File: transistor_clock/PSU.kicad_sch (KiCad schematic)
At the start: 15 parts, among them Q125 TIP41, Q27 MMBT3904

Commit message: seconds_minor_wrapup
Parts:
- C74, C76, D255, RV1: Assembly (none) -> False
- D296: footprint (none) -> Package_SO:SO-4_4.4x4.3mm_P2.54mm; Assembly (none) -> False
- D297: footprint (none) -> Diode_SMD:D_MiniMELF; Assembly (none) -> False
- Q123, Q124: renamed from Q27; Assembly (none) -> True; LCSC_PN (none) -> C20526; Price (none) -> 0.0094
- R20: renamed from R45; LCSC_PN (none) -> C21190; Price (none) -> 0.0005
- renumbered R45 to R20, R20 to R243, R41 to R253

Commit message: seconds_major_wrapup
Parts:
- R20: Assembly (none) -> True
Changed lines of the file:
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@@
       (effects (font (size 1.27 1.27)) hide)
     )
-    (property "Assembly" "" (at 157.48 76.2 0)
+    (property "Assembly" "True" (at 157.48 76.2 0)
       (effects (font (size 1.27 1.27)) hide)
     )
@@
       (effects (font (size 1.27 1.27)) hide)
     )
-    (property "Assembly" "" (at 132.08 77.47 0)
-      (effects (font (size 1.27 1.27)) hide)
-    )
+    (property "Assembly" "True" (at 132.08 77.47 0)
+      (effects (font (size 1.27 1.27)) hide)
+    )

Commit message: added content
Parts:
- C76: value 100u -> 10u; footprint (none) -> Capacitor_SMD:C_0805_2012Metric; Assembly False -> True; LCSC_PN (none) -> C15850; Price (none) -> 0.0105

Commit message: added content
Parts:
- removed D255: LED, LED_SMD:LED_0603_1608Metric, symbol Device:LED
- removed Q124: MMBT3904, Package_TO_SOT_SMD:SOT-23, symbol Transistor_BJT:MMBT3904
- removed R20 (x2): 1k, Resistor_SMD:R_0603_1608Metric, symbol Device:R
- removed R243, R253: 500, Resistor_SMD:R_0603_1608Metric, symbol Device:R
- removed RV1: 500, symbol Device:R_Potentiometer
- added C60, C65, C66, C81, C82: 10u, Capacitor_SMD:C_1206_3216Metric, symbol Device:C_Polarized
- added C61: 10u, Capacitor_SMD:C_0805_2012Metric, symbol Device:C_Polarized
- added D144: 1N4148W, Diode_SMD:D_SOD-123, symbol Device:D
- C74: footprint (none) -> Capacitor_THT:CP_Radial_D10.0mm_P3.50mm
- C75: value 220u -> 10u; footprint (none) -> Capacitor_SMD:C_1206_3216Metric; Assembly (none) -> True; LCSC_PN (none) -> C13585; Price (none) -> 0.029
- D297: value D_Zener -> 11V
- Q125: footprint Package_TO_SOT_THT:TO-220-3_Vertical -> Package_TO_SOT_THT:TO-220-3_Horizontal_TabDown
- R20: value 500 -> 1k; Assembly (none) -> True; LCSC_PN (none) -> C21190; Price (none) -> 0.0005
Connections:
- net 12V_out: now also C61.1
- net GND: now also C60.2, C61.2, C65.2, C66.2, C81.2, C82.2
- net at Q123.1 (B): now also R20.2, C82.1, D144.2 (A)
- net at C75.1: now also C74.1, D296.1 (+), Q123.3 (C), Q125.2 (C), R20.1, C60.1, C65.1, C66.1, C81.1; no longer R20.2
- net at D297.1 (K): now also D144.1 (K)
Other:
- moved on the sheet: C76, D297, Q123, Q125, R20

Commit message: added content
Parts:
- added C83, C84, C97: 10u, Capacitor_SMD:C_1206_3216Metric, symbol Device:C_Polarized
- C74: value 10mF -> 220u
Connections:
- net GND: now also C83.2, C84.2, C97.2
- net at C60.1, C65.1, C66.1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: now also C83.1, C84.1, C97.1
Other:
- note added: "TODO check tran"
- note removed: "Check tran/replace with darlington?"
- moved on the sheet: C61, C75, C76, C82, D144, D297, Q123, Q125, R20

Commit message: added content
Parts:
- renumbered D144 to D139
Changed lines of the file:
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@@
   (symbol (lib_id "Device:D") (at 185.42 73.66 90) (unit 1)
     (in_bom yes) (on_board yes) (dnp no) (fields_autoplaced)
-    (property "Reference" "D144" (at 187.452 73.0163 90)
+    (property "Reference" "D139" (at 187.452 73.0163 90)
       (effects (font (size 1.27 1.27)) (justify right))
     )
@@
     (instances
       (project "transistor_clock"
-        (path "/b32464e6-c3c7-41da-ac79-643e545075e2/7ea6f02c-98d6-4cc3-9d12-1d5708d2f4a9/cadfc701-a229-43d0-bd3d-a4fb656a51ec/cdd346a2-af99-4cba-a870-25a15852fcab"
-          (reference "D144") (unit 1)
+        (path "/b32464e6-c3c7-41da-ac79-643e545075e2/fc84256b-6a0b-4a66-8a9d-3464331d8c4b/cadfc701-a229-43d0-bd3d-a4fb656a51ec/cdd346a2-af99-4cba-a870-25a15852fcab"
+          (reference "D139") (unit 1)
+        )
+        (path "/b32464e6-c3c7-41da-ac79-643e545075e2/fc837116-7951-4754-b134-6b29a9ce0d20/f7326efb-cfc5-42e3-bc99-3d82c7965823/09ad6700-0804-43e5-8393-34ed739096ca"
+          (reference "D302") (unit 1)
+        )
+        (path "/b32464e6-c3c7-41da-ac79-643e545075e2/fc84256b-6a0b-4a66-8a9d-3464331d8c4b/cadfc701-a229-43d0-bd3d-a4fb656a51ec/7f89f7e8-4eb0-459f-8749-acca2517c0c8"
+          (reference "D256") (unit 1)
+        )
+        (path "/b32464e6-c3c7-41da-ac79-643e545075e2/369b0561-6154-45b1-b267-ff673911a7b5/f7326efb-cfc5-42e3-bc99-3d82c7965823/96f657b6-18d3-41c6-a281-d64d12e655e8"
+          (reference "D298") (unit 1)
+        )
+        (path "/b32464e6-c3c7-41da-ac79-643e545075e2/369b0561-6154-45b1-b267-ff673911a7b5/f7326efb-cfc5-42e3-bc99-3d82c7965823/4e2cbe41-dc2d-4674-8cd4-acbdb09cdaf2"
+          (reference "D299") (unit 1)
+        )
+        (path "/b32464e6-c3c7-41da-ac79-643e545075e2/fc84256b-6a0b-4a66-8a9d-3464331d8c4b/cadfc701-a229-43d0-bd3d-a4fb656a51ec/0211eb0b-97a3-455a-a4b9-49336bda2571"
+          (reference "D141") (unit 1)
+        )
+        (path "/b32464e6-c3c7-41da-ac79-643e545075e2/7ea6f02c-98d6-4cc3-9d12-1d5708d2f4a9/cadfc701-a229-43d0-bd3d-a4fb656a51ec/0211eb0b-97a3-455a-a4b9-49336bda2571"
+          (reference "D142") (unit 1)
+        )
+        (path "/b32464e6-c3c7-41da-ac79-643e545075e2/fc837116-7951-4754-b134-6b29a9ce0d20/f7326efb-cfc5-42e3-bc99-3d82c7965823/df4d8492-d3b8-496d-b6ec-19710c264b23"
+          (reference "D303") (unit 1)
+        )
+        (path "/b32464e6-c3c7-41da-ac79-643e545075e2/fc84256b-6a0b-4a66-8a9d-3464331d8c4b/cadfc701-a229-43d0-bd3d-a4fb656a51ec/28fcebf3-a860-4674-8b07-a85c9eaa7b85"
+          (reference "D58") (unit 1)
+        )
+        (path "/b32464e6-c3c7-41da-ac79-643e545075e2/369b0561-6154-45b1-b267-ff673911a7b5/f7326efb-cfc5-42e3-bc99-3d82c7965823/ef0016b9-6554-41fb-9e38-165a2c96731c"
+          (reference "D301") (unit 1)
+        )
+        (path "/b32464e6-c3c7-41da-ac79-643e545075e2/fc84256b-6a0b-4a66-8a9d-3464331d8c4b/cadfc701-a229-43d0-bd3d-a4fb656a51ec/97296d8c-1e14-436e-9883-ea2ff2d821d3"
+          (reference "D281") (unit 1)
+        )
+        (path "/b32464e6-c3c7-41da-ac79-643e545075e2/fc84256b-6a0b-4a66-8a9d-3464331d8c4b/cadfc701-a229-43d0-bd3d-a4fb656a51ec"
+          (reference "D22") (unit 1)
+        )
+        (path "/b32464e6-c3c7-41da-ac79-643e545075e2/fc837116-7951-4754-b134-6b29a9ce0d20/f7326efb-cfc5-42e3-bc99-3d82c7965823/96f657b6-18d3-41c6-a281-d64d12e655e8"
+          (reference "D304") (unit 1)
+        )
+        (path "/b32464e6-c3c7-41da-ac79-643e545075e2/fc837116-7951-4754-b134-6b29a9ce0d20/f7326efb-cfc5-42e3-bc99-3d82c7965823/4e2cbe41-dc2d-4674-8cd4-acbdb09cdaf2"
+          (reference "D305") (unit 1)
+        )
+        (path "/b32464e6-c3c7-41da-ac79-643e545075e2/fc837116-7951-4754-b134-6b29a9ce0d20/f7326efb-cfc5-42e3-bc99-3d82c7965823/b586ad64-4356-4c54-8b14-a38f5ba9b5b3"
+          (reference "D306") (unit 1)
+        )
+        (path "/b32464e6-c3c7-41da-ac79-643e545075e2/fc837116-7951-4754-b134-6b29a9ce0d20/f7326efb-cfc5-42e3-bc99-3d82c7965823/ef0016b9-6554-41fb-9e38-165a2c96731c"
+          (reference "D307") (unit 1)
+        )
+        (path "/b32464e6-c3c7-41da-ac79-643e545075e2/369b0561-6154-45b1-b267-ff673911a7b5/f7326efb-cfc5-42e3-bc99-3d82c7965823/09ad6700-0804-43e5-8393-34ed739096ca"
+          (reference "D296") (unit 1)
+        )
+        (path "/b32464e6-c3c7-41da-ac79-643e545075e2/369b0561-6154-45b1-b267-ff673911a7b5/f7326efb-cfc5-42e3-bc99-3d82c7965823/df4d8492-d3b8-496d-b6ec-19710c264b23"
+          (reference "D297") (unit 1)
+        )
+        (path "/b32464e6-c3c7-41da-ac79-643e545075e2/fc84256b-6a0b-4a66-8a9d-3464331d8c4b/cadfc701-a229-43d0-bd3d-a4fb656a51ec/96e64c28-7545-40f7-aaf3-a4fd012e71a7"
+          (reference "D127") (unit 1)
         )
         (path "/b32464e6-c3c7-41da-ac79-643e545075e2/fc84256b-6a0b-4a66-8a9d-3464331d8c4b/cadfc701-a229-43d0-bd3d-a4fb656a51ec/eec5b1ac-93db-432a-87e8-e2b0529019a6"
@@
           (reference "D285") (unit 1)
         )
-        (path "/b32464e6-c3c7-41da-ac79-643e545075e2/fc84256b-6a0b-4a66-8a9d-3464331d8c4b/cadfc701-a229-43d0-bd3d-a4fb656a51ec/96e64c28-7545-40f7-aaf3-a4fd012e71a7"
-          (reference "D127") (unit 1)
+        (path "/b32464e6-c3c7-41da-ac79-643e545075e2/7ea6f02c-98d6-4cc3-9d12-1d5708d2f4a9/cadfc701-a229-43d0-bd3d-a4fb656a51ec/cdd346a2-af99-4cba-a870-25a15852fcab"
+          (reference "D144") (unit 1)
         )
         (path "/b32464e6-c3c7-41da-ac79-643e545075e2"
@@
           (reference "D300") (unit 1)
         )
-        (path "/b32464e6-c3c7-41da-ac79-643e545075e2/369b0561-6154-45b1-b267-ff673911a7b5/f7326efb-cfc5-42e3-bc99-3d82c7965823/ef0016b9-6554-41fb-9e38-165a2c96731c"
-          (reference "D301") (unit 1)
-        )
-        (path "/b32464e6-c3c7-41da-ac79-643e545075e2/fc837116-7951-4754-b134-6b29a9ce0d20/f7326efb-cfc5-42e3-bc99-3d82c7965823/09ad6700-0804-43e5-8393-34ed739096ca"
-          (reference "D302") (unit 1)
-        )
-        (path "/b32464e6-c3c7-41da-ac79-643e545075e2/fc84256b-6a0b-4a66-8a9d-3464331d8c4b/cadfc701-a229-43d0-bd3d-a4fb656a51ec/7f89f7e8-4eb0-459f-8749-acca2517c0c8"
-          (reference "D256") (unit 1)
-        )
-        (path "/b32464e6-c3c7-41da-ac79-643e545075e2/369b0561-6154-45b1-b267-ff673911a7b5/f7326efb-cfc5-42e3-bc99-3d82c7965823/96f657b6-18d3-41c6-a281-d64d12e655e8"
-          (reference "D298") (unit 1)
-        )
-        (path "/b32464e6-c3c7-41da-ac79-643e545075e2/369b0561-6154-45b1-b267-ff673911a7b5/f7326efb-cfc5-42e3-bc99-3d82c7965823/4e2cbe41-dc2d-4674-8cd4-acbdb09cdaf2"
-          (reference "D299") (unit 1)
-        )
-        (path "/b32464e6-c3c7-41da-ac79-643e545075e2/fc84256b-6a0b-4a66-8a9d-3464331d8c4b/cadfc701-a229-43d0-bd3d-a4fb656a51ec/0211eb0b-97a3-455a-a4b9-49336bda2571"
-          (reference "D141") (unit 1)
-        )
-        (path "/b32464e6-c3c7-41da-ac79-643e545075e2/7ea6f02c-98d6-4cc3-9d12-1d5708d2f4a9/cadfc701-a229-43d0-bd3d-a4fb656a51ec/0211eb0b-97a3-455a-a4b9-49336bda2571"
-          (reference "D142") (unit 1)
-        )
-        (path "/b32464e6-c3c7-41da-ac79-643e545075e2/fc837116-7951-4754-b134-6b29a9ce0d20/f7326efb-cfc5-42e3-bc99-3d82c7965823/df4d8492-d3b8-496d-b6ec-19710c264b23"
-          (reference "D303") (unit 1)
-        )
-        (path "/b32464e6-c3c7-41da-ac79-643e545075e2/fc84256b-6a0b-4a66-8a9d-3464331d8c4b/cadfc701-a229-43d0-bd3d-a4fb656a51ec/28fcebf3-a860-4674-8b07-a85c9eaa7b85"
-          (reference "D58") (unit 1)
-        )
-        (path "/b32464e6-c3c7-41da-ac79-643e545075e2/fc84256b-6a0b-4a66-8a9d-3464331d8c4b/cadfc701-a229-43d0-bd3d-a4fb656a51ec/cdd346a2-af99-4cba-a870-25a15852fcab"
-          (reference "D139") (unit 1)
-        )
-        (path "/b32464e6-c3c7-41da-ac79-643e545075e2/fc84256b-6a0b-4a66-8a9d-3464331d8c4b/cadfc701-a229-43d0-bd3d-a4fb656a51ec/97296d8c-1e14-436e-9883-ea2ff2d821d3"
-          (reference "D281") (unit 1)
-        )
-        (path "/b32464e6-c3c7-41da-ac79-643e545075e2/fc84256b-6a0b-4a66-8a9d-3464331d8c4b/cadfc701-a229-43d0-bd3d-a4fb656a51ec"
-          (reference "D22") (unit 1)
-        )
-        (path "/b32464e6-c3c7-41da-ac79-643e545075e2/fc837116-7951-4754-b134-6b29a9ce0d20/f7326efb-cfc5-42e3-bc99-3d82c7965823/96f657b6-18d3-41c6-a281-d64d12e655e8"
-          (reference "D304") (unit 1)
-        )
-        (path "/b32464e6-c3c7-41da-ac79-643e545075e2/fc837116-7951-4754-b134-6b29a9ce0d20/f7326efb-cfc5-42e3-bc99-3d82c7965823/4e2cbe41-dc2d-4674-8cd4-acbdb09cdaf2"
-          (reference "D305") (unit 1)
-        )
-        (path "/b32464e6-c3c7-41da-ac79-643e545075e2/fc837116-7951-4754-b134-6b29a9ce0d20/f7326efb-cfc5-42e3-bc99-3d82c7965823/b586ad64-4356-4c54-8b14-a38f5ba9b5b3"
-          (reference "D306") (unit 1)
-        )
-        (path "/b32464e6-c3c7-41da-ac79-643e545075e2/fc837116-7951-4754-b134-6b29a9ce0d20/f7326efb-cfc5-42e3-bc99-3d82c7965823/ef0016b9-6554-41fb-9e38-165a2c96731c"
-          (reference "D307") (unit 1)
-        )
-        (path "/b32464e6-c3c7-41da-ac79-643e545075e2/369b0561-6154-45b1-b267-ff673911a7b5/f7326efb-cfc5-42e3-bc99-3d82c7965823/09ad6700-0804-43e5-8393-34ed739096ca"
-          (reference "D296") (unit 1)
-        )
-        (path "/b32464e6-c3c7-41da-ac79-643e545075e2/369b0561-6154-45b1-b267-ff673911a7b5/f7326efb-cfc5-42e3-bc99-3d82c7965823/df4d8492-d3b8-496d-b6ec-19710c264b23"
-          (reference "D297") (unit 1)
-        )
       )

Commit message: a
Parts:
- removed C84, C97: 10u, Capacitor_SMD:C_1206_3216Metric, symbol Device:C_Polarized
- removed D139: 1N4148W, Diode_SMD:D_SOD-123, symbol Device:D
- removed D296: D_Bridge_+-AA, Package_SO:SO-4_4.4x4.3mm_P2.54mm, symbol Device:D_Bridge_+-AA
- removed Q123: MMBT3904, Package_TO_SOT_SMD:SOT-23, symbol Transistor_BJT:MMBT3904
- removed Q125: TIP41, Package_TO_SOT_THT:TO-220-3_Horizontal_TabDown, symbol Transistor_BJT:TIP41
- removed R20: 1k, Resistor_SMD:R_0603_1608Metric, symbol Device:R
- added D256 (x3), D286 (x3): 1N4148W, Diode_SMD:D_SOD-123, symbol Device:D
- added Q123: VN3205, Package_TO_SOT_SMD:SOT-89-3, symbol Device:Q_NMOS_GDS
- added Q124: MMBT5551, Package_TO_SOT_SMD:SOT-23, symbol Transistor_BJT:MMBT3904
- added R20 (x2): 100k, Resistor_SMD:R_0603_1608Metric, symbol Device:R
- added R20: 22k, Resistor_SMD:R_0603_1608Metric, symbol Device:R
- added R20 (x2): 2k2, Resistor_SMD:R_0603_1608Metric, symbol Device:R
- added R20: 10k, Resistor_SMD:R_0603_1608Metric, symbol Device:R
- C60: footprint Capacitor_SMD:C_1206_3216Metric -> Capacitor_SMD:C_0805_2012Metric; LCSC_PN C13585 -> C15850; Price 0.029 -> 0.0105
- C65, C66, C75, C81, C82, C83: value 10u -> 470u; footprint Capacitor_SMD:C_1206_3216Metric -> Capacitor_SMD:CP_Elec_8x5.4; Assembly True -> OK; LCSC_PN C13585 -> (none); Price 0.029 -> (none)
- C74: value 220u -> 470u; footprint Capacitor_THT:CP_Radial_D10.0mm_P3.50mm -> Capacitor_SMD:CP_Elec_8x5.4; Assembly False -> OK
- D297: value 11V -> 3V3; Assembly False -> OK
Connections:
- net 12V_out: now also Q123.3 (S), R20.1
- net AC1: now also C66.2, C74.1, D256.2 (A), D286.1 (K), Q123.2 (D), R20.1
- net AC2: now also C65.1, C81.2
- net GND: now also D286.2 (A), R20.2, R20.2; no longer C65.2, C66.2, C75.2, C81.2, C82.2
- net Vleds: now also C82.1, D256.1 (K), R20.1
- net at D297.1 (K): now also Q124.2 (E)
- new net: C66.1, D256.1 (K), D286.2 (A)
- new net: C75.2, C81.1, D256.1 (K), D256.2 (A)
- new net: C82.2, C83.1, R20.1, R20.2
- new net: Q124.1 (B), R20.1, R20.2
- new net: C60.1, R20.2, R20.2
- new net: Q123.1 (G), Q124.3 (C), R20.1
- new net: C75.1, D256.2 (A), D286.1 (K)
- new net Sync: C65.2, D286.1 (K), D286.2 (A)
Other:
- note added: "15V"
- note added: "25V"
- note added: "70V"
- note removed: "TODO MB10S 0.5A SOIC4 sufficient?"
- moved on the sheet: C74, D297

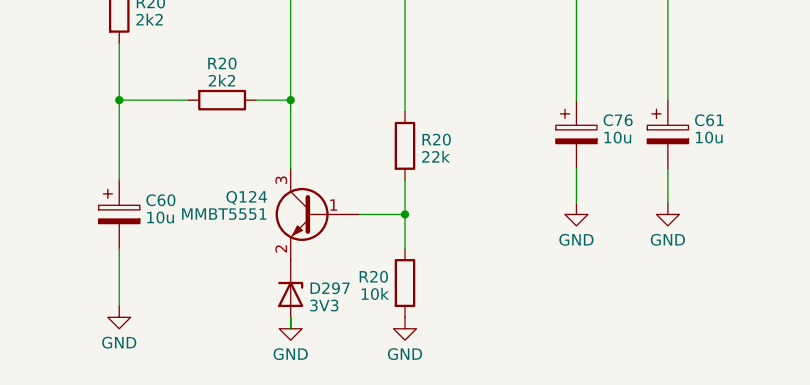
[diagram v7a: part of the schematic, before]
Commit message: added svg viz
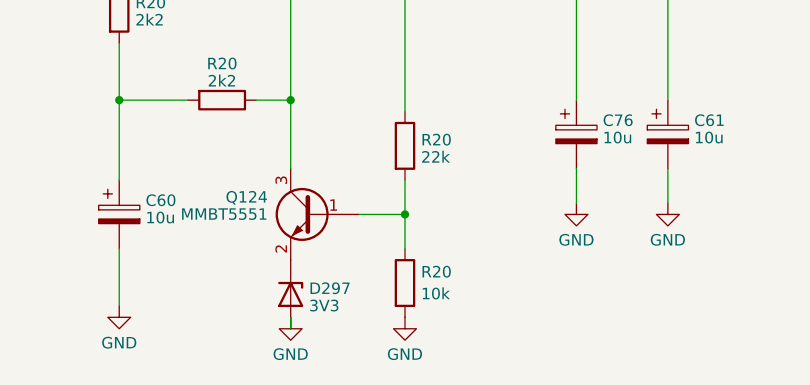
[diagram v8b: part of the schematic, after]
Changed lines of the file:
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@@
   (symbol (lib_id "Device:R") (at 198.12 93.98 0) (unit 1)
     (in_bom yes) (on_board yes) (dnp no) (fields_autoplaced)
-    (property "Reference" "R20" (at 196.3421 93.3363 0)
-      (effects (font (size 1.27 1.27)) (justify right))
+    (property "Reference" "R20" (at 199.898 92.7679 0)
+      (effects (font (size 1.27 1.27)) (justify left))
     )
-    (property "Value" "10k" (at 196.3421 95.2573 0)
-      (effects (font (size 1.27 1.27)) (justify right))
+    (property "Value" "10k" (at 199.898 95.1921 0)
+      (effects (font (size 1.27 1.27)) (justify left))
     )
     (property "Footprint" "Resistor_SMD:R_0603_1608Metric" (at 196.342 93.98 90)
